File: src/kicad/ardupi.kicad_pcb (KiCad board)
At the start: 2 copper layers, 65 x 30 mm, 50 parts, among them J1 GPIO_CONNECTOR, U1 MPU-9250, U2 ULN2803ADW, U4 PCA9685BS

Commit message: +adc
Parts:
- added C6: 10uF, Capacitor_SMD:C_0402_1005Metric, F.Cu at (258.1, 111.3)
- added COMPASS1: CONN_04POLAR, Connectors:MOLEX-1X4, F.Cu at (226.3, 125.5)
- added I2C1: CONN_04POLAR, Connectors:MOLEX-1X4, F.Cu at (230.1, 110.0)
- added J2: CONN_02POLAR, Connectors:MOLEX-1X2, F.Cu at (223.8, 135.3)
- added J3: 6_PIN_SERIAL_TARGET, Connectors:1X06, F.Cu at (198.5, 127.6)
- added NOTIFY1: CONN_05, Connectors:1X05, F.Cu at (198.5, 131.3)
- added R32: 470 KΩ, Resistor_SMD:R_0402_1005Metric, F.Cu at (221.5, 141.5)
- added R33: 470 Ω, Resistor_SMD:R_0402_1005Metric, F.Cu at (223.4, 139.4)
- added R34: 10KΩ, Resistor_SMD:R_0402_1005Metric, F.Cu at (232.5, 131.6)
- added R35: 10KΩ, Resistor_SMD:R_0402_1005Metric, F.Cu at (252.3, 107.3)
- added R37: 10KΩ, Resistor_SMD:R_0402_1005Metric, F.Cu at (242.4, 122.3)
- added R38: 10KΩ, Resistor_SMD:R_0402_1005Metric, F.Cu at (255.2, 107.3)
- added RCIN1: Conn_01x10, Connector_PinHeader_2.54mm:PinHeader_1x10_P2.54mm_Vertical, F.Cu at (171.8, 137.7)
- added SERIAL1: CONN_04POLAR, Connectors:MOLEX-1X4, F.Cu at (241.4, 110.0)
- added SPI1: CONN_06POLAR, Connectors:MOLEX-1X6, F.Cu at (213.8, 110.0)
- added U6: ADS1115IRUGR, ADS1115IRUGR:ADS1115IRUGR, F.Cu at (179.1, 141.9)
- C1, C2, C3, C4, C5: footprint Capacitor_SMD:C_0201_0603Metric_Pad0.64x0.40mm_HandSolder -> Capacitor_SMD:C_0402_1005Metric
- R1, R10, R11, R12, R13, R14, R15, R16, R17, R18, R19, R20, R21, R22, R23, R8, R9: footprint Resistor_SMD:R_0805_2012Metric -> Resistor_SMD:R_0402_1005Metric
- R2: value 0 Ohm -> 10K; footprint Resistor_SMD:R_0805_2012Metric -> Resistor_SMD:R_0402_1005Metric_Pad0.72x0.64mm_HandSolder
- R24, R25, R26, R27, R28, R29, R30, R31: footprint Resistor_SMD:R_0603_1608Metric_Pad0.98x0.95mm_HandSolder -> Resistor_SMD:R_0402_1005Metric
- R3, R4, R5, R6, R7: value 0 Ohm -> 10K; footprint Resistor_SMD:R_0805_2012Metric -> Resistor_SMD:R_0402_1005Metric
- moved C2 53.2 mm to (251.9, 115.3)
- moved R7 44.8 mm to (212.7, 141.5)
- moved U1 44.5 mm to (238.3, 123.9)
- moved R28 43.7 mm to (215.6, 141.5)
- moved JP2 42.5 mm to (229.5, 117.5)
- moved R31 41.4 mm to (252.3, 109.3)
- moved R18 40.8 mm to (249.0, 114.1)
- moved R5 39.8 mm to (242.4, 124.3)
- moved R12 39.7 mm to (229.6, 137.5)
- moved JP4 39.4 mm to (218.8, 127.3)
- moved R8 38.4 mm to (232.5, 133.6)
- moved R10 37.4 mm to (255.2, 109.3)
- moved JP3 37.0 mm to (216.2, 136.1)
- moved R30 36.9 mm to (255.2, 111.3)
- moved R25 36.6 mm to (218.6, 141.5)
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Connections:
- U2 pad 1: unconnected-(U2-1B) -> /BUZZER
- U2 pad 10: unconnected-(U2-COM) -> /V_EXT
- U2 pad 11: unconnected-(U2-8C) -> /LED_3_OUT
- U2 pad 12: unconnected-(U2-7C) -> /LED_3_OUT
- U2 pad 13: unconnected-(U2-6C) -> /LED_2_OUT
- U2 pad 14: unconnected-(U2-5C) -> /LED_2_OUT
- U2 pad 15: unconnected-(U2-4C) -> /LED_1_OUT
- U2 pad 16: unconnected-(U2-3C) -> /LED_1_OUT
- U2 pad 17: unconnected-(U2-2C) -> /BUZZER_OUT
- U2 pad 18: unconnected-(U2-1C) -> /BUZZER_OUT
- U2 pad 2: unconnected-(U2-2B) -> /BUZZER
- U2 pad 3: unconnected-(U2-3B) -> /LED_1
- U2 pad 4: unconnected-(U2-4B) -> /LED_1
- U2 pad 5: unconnected-(U2-5B) -> /LED_2
- U2 pad 6: unconnected-(U2-6B) -> /LED_2
- U2 pad 7: unconnected-(U2-7B) -> /LED_3
- U2 pad 8: unconnected-(U2-8B) -> /LED_3
- U2 pad 9: unconnected-(U2-GND) -> GND

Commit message: fix
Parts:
- removed C6: 10uF, Capacitor_SMD:C_0402_1005Metric
- removed COMPASS1, I2C1, SERIAL1: CONN_04POLAR, Connectors:MOLEX-1X4
- removed JP2, JP3, JP4: HEADER-3X04, header-3x4:3X04
- removed NOTIFY1: CONN_05, Connectors:1X05
- removed R32: 470 KΩ, Resistor_SMD:R_0402_1005Metric
- removed R33: 470 Ω, Resistor_SMD:R_0402_1005Metric
- removed R34, R35, R37, R38: 10KΩ, Resistor_SMD:R_0402_1005Metric
- removed RCIN1: Conn_01x10, Connector_PinHeader_2.54mm:PinHeader_1x10_P2.54mm_Vertical
- removed SPI1: CONN_06POLAR, Connectors:MOLEX-1X6
- added U3: MPU-9250, mpu9250:mpu9250, F.Cu at (227.7, 125.0)
- C1, C2, C3, C4, C5: footprint Capacitor_SMD:C_0402_1005Metric -> Capacitor_SMD:C_0201_0603Metric_Pad0.64x0.40mm_HandSolder
- J2: value CONN_02POLAR -> Conn_02x16_Top_Bottom; footprint Connectors:MOLEX-1X2 -> Connector_PinHeader_2.54mm:PinHeader_2x16_P2.54mm_Vertical
- J3: value 6_PIN_SERIAL_TARGET -> Conn_01x16; footprint Connectors:1X06 -> Connector_PinHeader_2.54mm:PinHeader_1x16_P2.54mm_Vertical
- JP1: footprint header-3x4:3X04 -> Adafruit PCA9685 rev C:3X04
- R1, R10, R11, R12, R13, R14, R15, R16, R17, R18, R19, R20, R21, R22, R23, R8, R9: footprint Resistor_SMD:R_0402_1005Metric -> Resistor_SMD:R_0805_2012Metric
- R2: value 10K -> 0 Ohm; footprint Resistor_SMD:R_0402_1005Metric_Pad0.72x0.64mm_HandSolder -> Resistor_SMD:R_0805_2012Metric
- R24, R25, R26, R27, R28, R29, R30, R31: footprint Resistor_SMD:R_0402_1005Metric -> Resistor_SMD:R_0603_1608Metric_Pad0.98x0.95mm_HandSolder
- R3, R4, R5, R6, R7: value 10K -> 0 Ohm; footprint Resistor_SMD:R_0402_1005Metric -> Resistor_SMD:R_0805_2012Metric
- moved R21 131.3 mm to (123.7, 137.6), turned to 90 degrees
- moved R18 120.1 mm to (131.3, 137.6), turned to 90 degrees
- moved R11 113.2 mm to (149.1, 137.6), turned to 90 degrees
- moved R15 112.2 mm to (138.9, 137.6), turned to 90 degrees
- moved R23 111.2 mm to (118.5, 137.7), turned to 90 degrees
- moved U4 111.1 mm to (128.7, 127.6), turned to -90 degrees
- moved R22 108.5 mm to (121.1, 137.6), turned to 90 degrees
- moved R9 107.8 mm to (154.1, 137.6), turned to 90 degrees
- moved R10 107.4 mm to (151.6, 137.6), turned to 90 degrees
- moved R20 105.8 mm to (126.2, 137.6), turned to 90 degrees
- moved R17 104.1 mm to (133.8, 137.6), turned to 90 degrees
- moved R13 102.5 mm to (144.0, 137.6), turned to 90 degrees
- moved R19 100.4 mm to (128.7, 137.6), turned to 90 degrees
- moved R16 89.9 mm to (136.4, 137.6), turned to 90 degrees
- moved R14 88.2 mm to (141.4, 137.6), turned to 90 degrees
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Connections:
- J2 pad 1: /SRVO_EN -> Net-(J2-Pad1)
- J2 pad 2: Net-(J2-Pad2) -> /PWM1
- J3 pad 1: (no net) -> Net-(J3-Pad1)
- J3 pad 2: (no net) -> Net-(J3-Pad1)
- J3 pad 3: (no net) -> Net-(J3-Pad1)
- J3 pad 4: (no net) -> Net-(J3-Pad1)
- J3 pad 5: (no net) -> Net-(J3-Pad1)
- J3 pad 6: (no net) -> Net-(J3-Pad1)
- JP1 pad 1: Net-(JP1-Pad1) -> /PWM1
- JP1 pad 10: Net-(JP1-Pad10) -> /PWM4
- JP1 pad 11: +5V -> /+V_SRVO
- JP1 pad 2: +5V -> /+V_SRVO
- JP1 pad 4: Net-(JP1-Pad4) -> /PWM2
- JP1 pad 5: +5V -> /+V_SRVO
- JP1 pad 7: Net-(JP1-Pad7) -> /PWM3
- JP1 pad 8: +5V -> /+V_SRVO
- R10 pad 1: Net-(JP1-Pad7) -> /PWM3
- R10 pad 2: /PWM3 -> Net-(R10-Pad2)
- R11 pad 1: Net-(JP1-Pad10) -> /PWM4
- R11 pad 2: /PWM4 -> Net-(R11-Pad2)
- R12 pad 1: Net-(JP4-Pad1) -> /PWM5
- R12 pad 2: /PWM5 -> Net-(R12-Pad2)
- R13 pad 1: Net-(JP4-Pad4) -> /PWM6
- R13 pad 2: /PWM6 -> Net-(R13-Pad2)
- R14 pad 1: Net-(JP4-Pad7) -> /PWM7
- R14 pad 2: /PWM7 -> Net-(R14-Pad2)
- R15 pad 1: Net-(JP4-Pad10) -> /PWM8
- R15 pad 2: /PWM8 -> Net-(R15-Pad2)
- R16 pad 2: unconnected-(JP2-Pad1) -> Net-(R16-Pad2)
- R17 pad 2: Net-(JP2-Pad4) -> Net-(R17-Pad2)
- R18 pad 2: Net-(JP2-Pad7) -> Net-(R18-Pad2)
- R19 pad 2: unconnected-(R19-Pad2) -> Net-(R19-Pad2)
- R20 pad 2: Net-(JP3-Pad1) -> Net-(R20-Pad2)
- R21 pad 2: Net-(JP3-Pad4) -> Net-(R21-Pad2)
- R22 pad 2: Net-(JP3-Pad7) -> Net-(R22-Pad2)
- R23 pad 2: Net-(JP3-Pad10) -> Net-(R23-Pad2)
- R8 pad 1: Net-(JP1-Pad1) -> /PWM1
- R8 pad 2: /PWM1 -> Net-(R8-Pad2)
- R9 pad 1: Net-(JP1-Pad4) -> /PWM2
- R9 pad 2: /PWM2 -> Net-(R9-Pad2)
- U2 pad 1: /BUZZER -> unconnected-(U2-Pad1)
- U2 pad 10: /V_EXT -> unconnected-(U2-Pad10)
- U2 pad 11: /LED_3_OUT -> unconnected-(U2-Pad11)
- U2 pad 12: /LED_3_OUT -> unconnected-(U2-Pad12)
- U2 pad 13: /LED_2_OUT -> unconnected-(U2-Pad13)
- U2 pad 14: /LED_2_OUT -> unconnected-(U2-Pad14)
- U2 pad 15: /LED_1_OUT -> unconnected-(U2-Pad15)
- U2 pad 16: /LED_1_OUT -> unconnected-(U2-Pad16)
- U2 pad 17: /BUZZER_OUT -> unconnected-(U2-Pad17)
- U2 pad 18: /BUZZER_OUT -> unconnected-(U2-Pad18)
- U2 pad 2: /BUZZER -> unconnected-(U2-Pad2)
- U2 pad 3: /LED_1 -> unconnected-(U2-Pad3)
- U2 pad 4: /LED_1 -> unconnected-(U2-Pad4)
- U2 pad 5: /LED_2 -> unconnected-(U2-Pad5)
- U2 pad 6: /LED_2 -> unconnected-(U2-Pad6)
- U2 pad 7: /LED_3 -> unconnected-(U2-Pad7)
- U2 pad 8: /LED_3 -> unconnected-(U2-Pad8)
- U2 pad 9: GND -> unconnected-(U2-Pad9)
- U4 pad 10: /PWM8 -> Net-(R15-Pad2)
- U4 pad 12: /PWM9 -> Net-(R16-Pad2)
- U4 pad 13: /PWM10 -> Net-(R17-Pad2)
- U4 pad 14: /PWM11 -> Net-(R18-Pad2)
- U4 pad 15: /PWM12 -> Net-(R19-Pad2)
- U4 pad 16: /PWM13 -> Net-(R20-Pad2)
- U4 pad 17: /PWM14 -> Net-(R21-Pad2)
- U4 pad 18: /PWM15 -> Net-(R22-Pad2)
- U4 pad 19: /PWM16 -> Net-(R23-Pad2)
- U4 pad 3: /PWM1 -> Net-(R8-Pad2)
- U4 pad 4: /PWM2 -> Net-(R9-Pad2)
- U4 pad 5: /PWM3 -> Net-(R10-Pad2)
- U4 pad 6: /PWM4 -> Net-(R11-Pad2)
- U4 pad 7: /PWM5 -> Net-(R12-Pad2)
- U4 pad 8: /PWM6 -> Net-(R13-Pad2)
- U4 pad 9: /PWM7 -> Net-(R14-Pad2)
- U6 pad 1: Net-(U6-ADDR) -> unconnected-(U6-Pad1)
- U6 pad 10: Net-(U6-SCL) -> unconnected-(U6-Pad10)
- U6 pad 4: /AIO0 -> unconnected-(U6-Pad4)
- U6 pad 5: /AIO1 -> unconnected-(U6-Pad5)
- U6 pad 6: /AIO2 -> unconnected-(U6-Pad6)
- U6 pad 9: Net-(U6-SDA) -> unconnected-(U6-Pad9)
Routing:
- net /PWM13: track 0.00 -> 8.08 mm
- net /PWM11: track 0.00 -> 7.92 mm
- net /PWM10: track 0.00 -> 7.76 mm
- net /PWM16: track 0.00 -> 7.70 mm
- net /PWM4: track 0.00 -> 7.68 mm
- net /PWM14: track 0.00 -> 7.68 mm
- net /PWM9: track 0.00 -> 7.68 mm
- net /PWM8: track 0.00 -> 7.68 mm
- net /PWM7: track 0.00 -> 7.68 mm
- net /PWM6: track 0.00 -> 7.68 mm
- net /PWM5: track 0.00 -> 7.68 mm
- net /PWM3: track 0.00 -> 7.68 mm
- net /PWM2: track 0.00 -> 7.68 mm
- net /PWM15: track 0.00 -> 7.68 mm
- net /PWM12: track 0.00 -> 7.68 mm
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
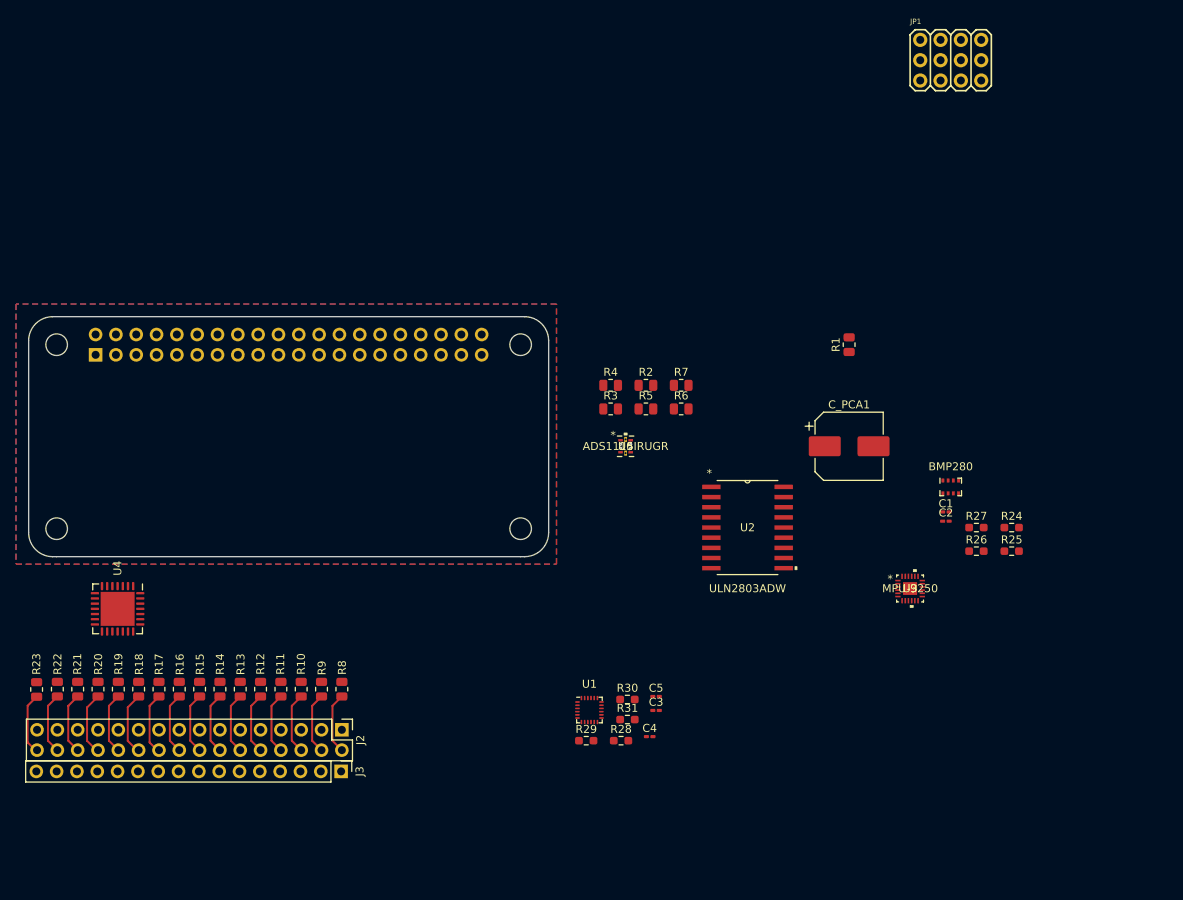
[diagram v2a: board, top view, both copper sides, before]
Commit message: fixed parts library, +3x4 header for pwm
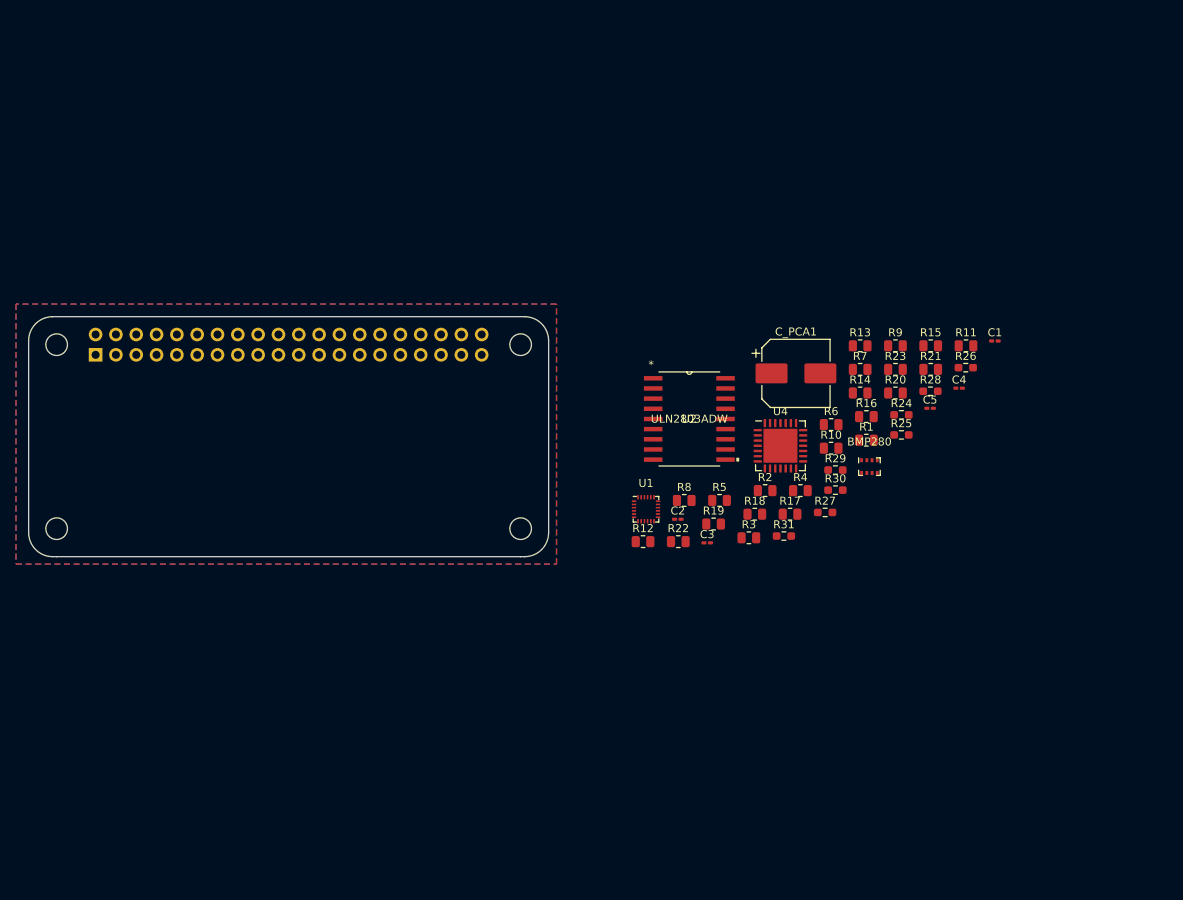
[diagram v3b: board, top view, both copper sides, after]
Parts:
- removed J2: Conn_02x16_Top_Bottom, Connector_PinHeader_2.54mm:PinHeader_2x16_P2.54mm_Vertical
- removed J3: Conn_01x16, Connector_PinHeader_2.54mm:PinHeader_1x16_P2.54mm_Vertical
- removed JP1: HEADER-3X04, Adafruit PCA9685 rev C:3X04
- removed U3: MPU-9250, mpu9250:mpu9250
- removed U6: ADS1115IRUGR, ADS1115IRUGR:ADS1115IRUGR
- moved R23 114.6 mm to (225.9, 97.7), turned to 0 degrees
- moved R21 113.9 mm to (230.3, 97.7), turned to 0 degrees
- moved R20 106.3 mm to (225.9, 100.6), turned to 0 degrees
- moved R15 101.0 mm to (230.3, 94.7), turned to 0 degrees
- moved R11 95.8 mm to (234.7, 94.7), turned to 0 degrees
- moved R16 92.4 mm to (222.3, 103.6), turned to 0 degrees
- moved R13 88.6 mm to (221.5, 94.7), turned to 0 degrees
- moved R14 88.2 mm to (221.5, 100.6), turned to 0 degrees
- moved U4 85.3 mm to (211.5, 107.2), turned to 0 degrees
- moved R9 83.6 mm to (225.9, 94.7), turned to 0 degrees
- moved R17 81.9 mm to (212.7, 115.8), turned to 0 degrees
- moved R18 80.1 mm to (208.3, 115.8), turned to 0 degrees
- moved R22 79.8 mm to (198.7, 119.2), turned to 0 degrees
- moved R19 77.2 mm to (203.2, 117.0), turned to 0 degrees
- moved R10 72.8 mm to (217.8, 107.5), turned to 0 degrees
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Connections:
- R10 pad 1: /PWM3 -> Net-(JP1-Pad7)
- R10 pad 2: Net-(R10-Pad2) -> /PWM3
- R11 pad 1: /PWM4 -> Net-(JP1-Pad10)
- R11 pad 2: Net-(R11-Pad2) -> /PWM4
- R12 pad 1: /PWM5 -> Net-(JP4-Pad1)
- R12 pad 2: Net-(R12-Pad2) -> /PWM5
- R13 pad 1: /PWM6 -> Net-(JP4-Pad4)
- R13 pad 2: Net-(R13-Pad2) -> /PWM6
- R14 pad 1: /PWM7 -> Net-(JP4-Pad7)
- R14 pad 2: Net-(R14-Pad2) -> /PWM7
- R15 pad 1: /PWM8 -> Net-(JP4-Pad10)
- R15 pad 2: Net-(R15-Pad2) -> /PWM8
- R16 pad 2: Net-(R16-Pad2) -> unconnected-(JP2-Pad1)
- R17 pad 2: Net-(R17-Pad2) -> Net-(JP2-Pad4)
- R18 pad 2: Net-(R18-Pad2) -> Net-(JP2-Pad7)
- R19 pad 2: Net-(R19-Pad2) -> unconnected-(R19-Pad2)
- R20 pad 2: Net-(R20-Pad2) -> Net-(JP3-Pad1)
- R21 pad 2: Net-(R21-Pad2) -> Net-(JP3-Pad4)
- R22 pad 2: Net-(R22-Pad2) -> Net-(JP3-Pad7)
- R23 pad 2: Net-(R23-Pad2) -> Net-(JP3-Pad10)
- R8 pad 1: /PWM1 -> Net-(JP1-Pad1)
- R8 pad 2: Net-(R8-Pad2) -> /PWM1
- R9 pad 1: /PWM2 -> Net-(JP1-Pad4)
- R9 pad 2: Net-(R9-Pad2) -> /PWM2
- U4 pad 10: Net-(R15-Pad2) -> /PWM8
- U4 pad 12: Net-(R16-Pad2) -> /PWM9
- U4 pad 13: Net-(R17-Pad2) -> /PWM10
- U4 pad 14: Net-(R18-Pad2) -> /PWM11
- U4 pad 15: Net-(R19-Pad2) -> /PWM12
- U4 pad 16: Net-(R20-Pad2) -> /PWM13
- U4 pad 17: Net-(R21-Pad2) -> /PWM14
- U4 pad 18: Net-(R22-Pad2) -> /PWM15
- U4 pad 19: Net-(R23-Pad2) -> /PWM16
- U4 pad 3: Net-(R8-Pad2) -> /PWM1
- U4 pad 4: Net-(R9-Pad2) -> /PWM2
- U4 pad 5: Net-(R10-Pad2) -> /PWM3
- U4 pad 6: Net-(R11-Pad2) -> /PWM4
- U4 pad 7: Net-(R12-Pad2) -> /PWM5
- U4 pad 8: Net-(R13-Pad2) -> /PWM6
- U4 pad 9: Net-(R14-Pad2) -> /PWM7
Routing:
- net /PWM13: track 8.08 -> 0.00 mm
- net /PWM11: track 7.92 -> 0.00 mm
- net /PWM10: track 7.76 -> 0.00 mm
- net /PWM16: track 7.70 -> 0.00 mm
- net /PWM4: track 7.68 -> 0.00 mm
- net /PWM14: track 7.68 -> 0.00 mm
- net /PWM9: track 7.68 -> 0.00 mm
- net /PWM8: track 7.68 -> 0.00 mm
- net /PWM7: track 7.68 -> 0.00 mm
- net /PWM6: track 7.68 -> 0.00 mm
- net /PWM5: track 7.68 -> 0.00 mm
- net /PWM3: track 7.68 -> 0.00 mm
- net /PWM2: track 7.68 -> 0.00 mm
- net /PWM15: track 7.68 -> 0.00 mm
- net /PWM12: track 7.68 -> 0.00 mm
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
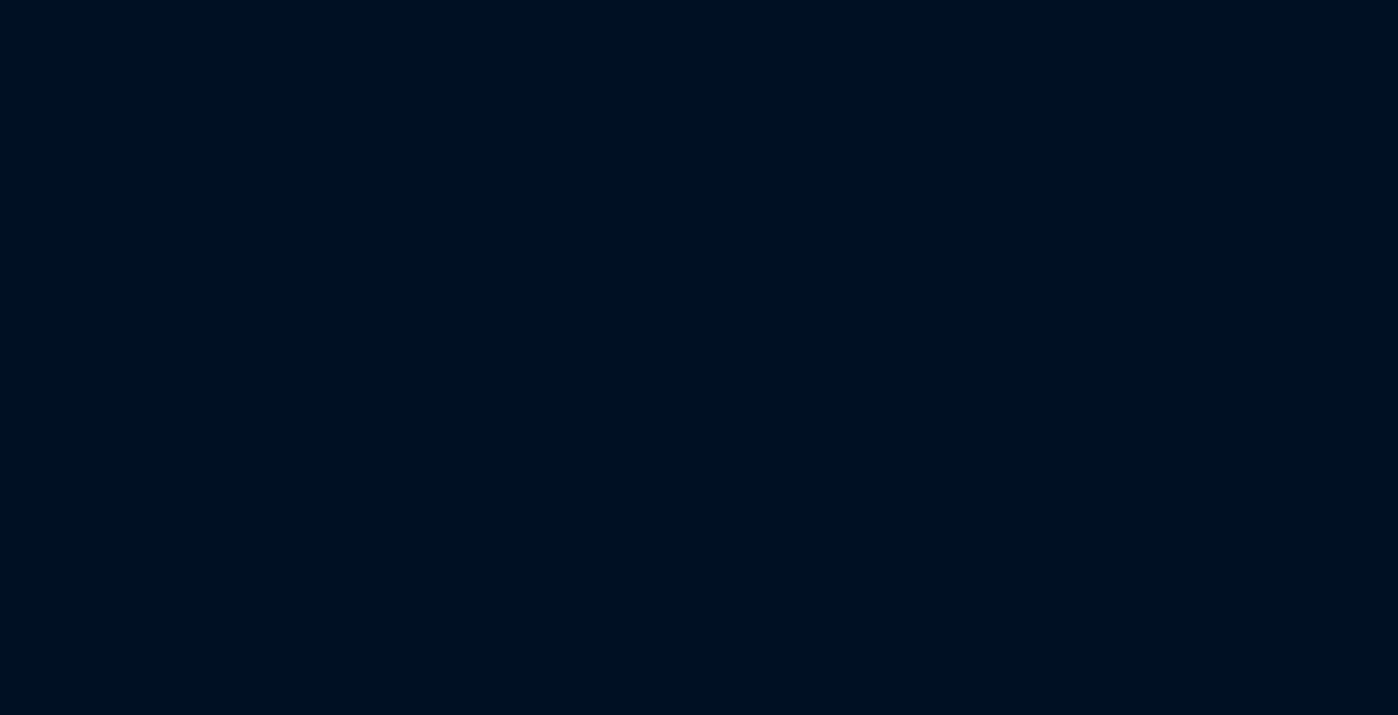
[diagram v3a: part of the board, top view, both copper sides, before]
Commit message: parts libary update: PWM 3x4 header should be correct
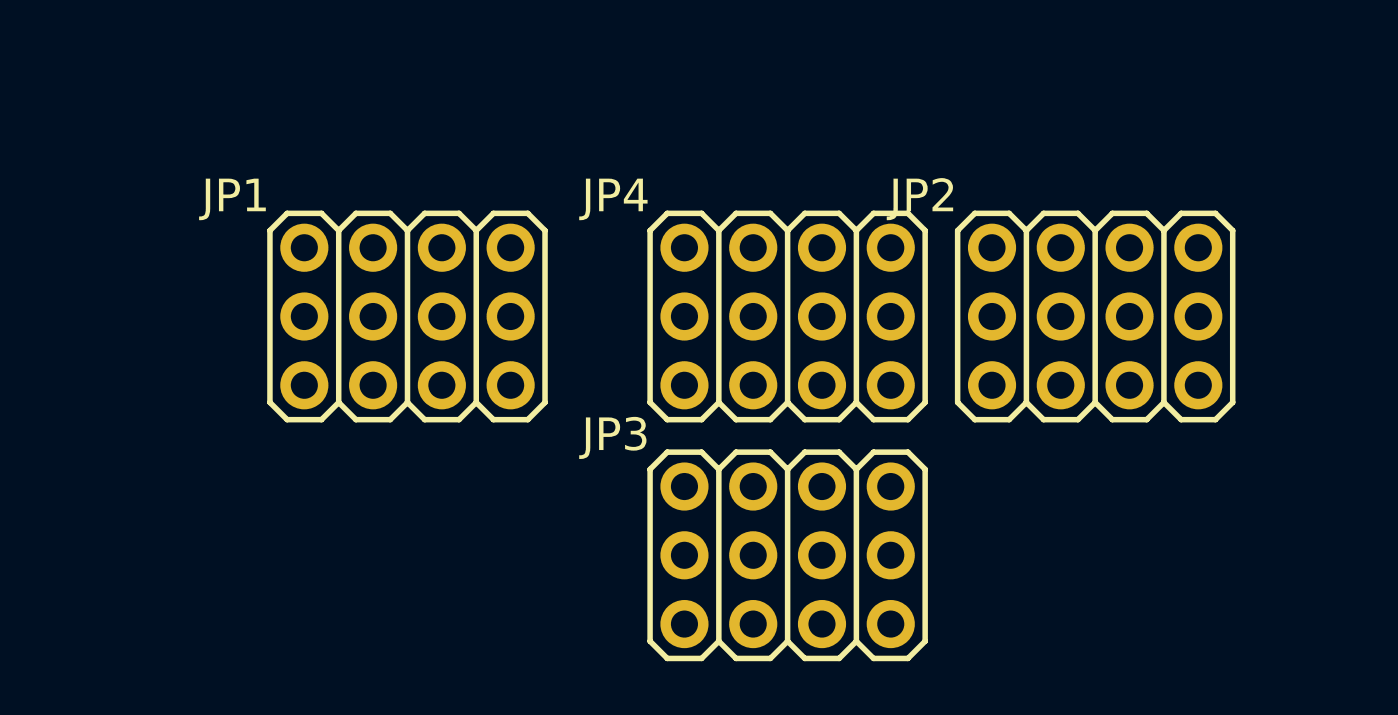
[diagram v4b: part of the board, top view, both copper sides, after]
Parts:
- added JP1: HEADER-3X04, header-3x4:3X04, F.Cu at (166.8, 137.7)
- added JP2: HEADER-3X04, header-3x4:3X04, F.Cu at (192.2, 137.7)
- added JP3: HEADER-3X04, header-3x4:3X04, F.Cu at (180.8, 146.6)
- added JP4: HEADER-3X04, header-3x4:3X04, F.Cu at (180.8, 137.7)
